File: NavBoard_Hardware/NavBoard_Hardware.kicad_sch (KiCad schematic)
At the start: 31 parts, among them J1 Conn_01x06_Male, U1 OKI-5V, U2 BHI160B, U3 ICM-20608-G, U4 OKI-3V3, U6 Raspberry_Pi

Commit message: Added title block info, adjusted powerpole connectors
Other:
- company: MRDT -> Missouri S&T Mars Rover Design Team
- title: NavBoard -> MRDT NavBoard
- moved on the sheet: Conn1A, Conn1B
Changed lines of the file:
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@@
   (paper "A4")
   (title_block
-    (title "NavBoard")
-    (rev "1")
-    (company "MRDT")
+    (title "MRDT NavBoard")
+    (date "2022-09-14")
+    (rev "2, 2023")
+    (company "Missouri S&T Mars Rover Design Team")
+    (comment 1 "Raspberry Pi Daughter Board")
+    (comment 2 "Contains Two Accelerometers & Connections To One UART GPS Module")
   )
   (junction (at 262.89 68.58) (diameter 0) (color 0 0 0 0)
@@
     (stroke (width 0) (type default) (color 0 0 0 0))
   )
+  (polyline (pts (xy 85.09 12.065) (xy 85.09 114.3))
+    (stroke (width 0) (type default) (color 0 0 0 0))
+  )
   (wire (pts (xy 246.38 148.59) (xy 246.38 151.13))
     (stroke (width 0) (type default) (color 0 0 0 0))
@@
     (stroke (width 0) (type default) (color 0 0 0 0))
   )
-  (wire (pts (xy 38.1 97.79) (xy 43.18 97.79))
+  (wire (pts (xy 36.83 97.79) (xy 31.75 97.79))
     (stroke (width 0) (type default) (color 0 0 0 0))
   )
@@
     (stroke (width 0) (type default) (color 0 0 0 0))
   )
-  (wire (pts (xy 66.04 97.79) (xy 71.12 97.79))
+  (wire (pts (xy 57.785 97.79) (xy 64.135 97.79))
     (stroke (width 0) (type default) (color 0 0 0 0))
   )
@@
     (stroke (width 0) (type default) (color 0 0 0 0))
   )
-  (wire (pts (xy 71.12 97.79) (xy 71.12 95.25))
+  (wire (pts (xy 64.135 97.79) (xy 64.135 95.25))
     (stroke (width 0) (type default) (color 0 0 0 0))
   )
@@
     (stroke (width 0) (type default) (color 0 0 0 0))
   )
-  (wire (pts (xy 43.18 97.79) (xy 43.18 100.33))
+  (wire (pts (xy 31.75 97.79) (xy 31.75 100.33))
     (stroke (width 0) (type default) (color 0 0 0 0))
   )
@@
     (effects (font (size 3.5052 3.5052) (thickness 0.701) bold italic) (justify left bottom))
   )
-  (text "Power" (at 43.18 20.32 0)
+  (text "Power" (at 38.735 20.32 0)
     (effects (font (size 3.5052 3.5052) (thickness 0.701) bold italic) (justify left bottom))
   )
@@
     (pin "1")
   )
-  (symbol (lib_id "MRDT_Connectors:AndersonPP") (at 27.94 100.33 0) (unit 1)
-    (in_bom yes) (on_board yes)
-    (property "Reference" "Conn1" (id 0) (at 33.2232 90.5002 0)
+  (symbol (lib_id "MRDT_Connectors:AndersonPP") (at 46.99 100.33 0) (mirror y) (unit 1)
+    (in_bom yes) (on_board yes)
+    (property "Reference" "Conn1" (id 0) (at 41.7068 90.5002 0)
       (effects (font (size 1.524 1.524)))
     )
-    (property "Value" "AndersonPP" (id 1) (at 33.2232 93.1926 0)
+    (property "Value" "AndersonPP" (id 1) (at 38.735 93.345 0)
       (effects (font (size 1.524 1.524)))
     )
-    (property "Footprint" "MRDT_Connectors:Anderson_2_Horizontal_Side_by_Side" (id 2) (at 24.13 114.3 0)
-      (effects (font (size 1.524 1.524)) hide)
-    )
-    (property "Datasheet" "" (id 3) (at 24.13 114.3 0)
-      (effects (font (size 1.524 1.524)) hide)
-    )
-    (pin "1")
-  )
-  (symbol (lib_id "MRDT_Connectors:AndersonPP") (at 55.88 100.33 0) (unit 2)
-    (in_bom yes) (on_board yes)
-    (property "Reference" "Conn1" (id 0) (at 61.1632 90.5002 0)
+    (property "Footprint" "MRDT_Connectors:Anderson_2_Horizontal_Side_by_Side" (id 2) (at 50.8 114.3 0)
+      (effects (font (size 1.524 1.524)) hide)
+    )
+    (property "Datasheet" "" (id 3) (at 50.8 114.3 0)
+      (effects (font (size 1.524 1.524)) hide)
+    )
+    (pin "1")
+  )
+  (symbol (lib_id "MRDT_Connectors:AndersonPP") (at 47.625 100.33 0) (unit 2)
+    (in_bom yes) (on_board yes)
+    (property "Reference" "Conn1" (id 0) (at 52.9082 90.5002 0)
       (effects (font (size 1.524 1.524)))
     )
-    (property "Value" "AndersonPP" (id 1) (at 61.1632 93.1926 0)
+    (property "Value" "AndersonPP" (id 1) (at 55.245 93.345 0)
       (effects (font (size 1.524 1.524)))
     )
-    (property "Footprint" "MRDT_Connectors:Anderson_2_Horizontal_Side_by_Side" (id 2) (at 52.07 114.3 0)
-      (effects (font (size 1.524 1.524)) hide)
-    )
-    (property "Datasheet" "" (id 3) (at 52.07 114.3 0)
+    (property "Footprint" "MRDT_Connectors:Anderson_2_Horizontal_Side_by_Side" (id 2) (at 43.815 114.3 0)
+      (effects (font (size 1.524 1.524)) hide)
+    )
+    (property "Datasheet" "" (id 3) (at 43.815 114.3 0)
       (effects (font (size 1.524 1.524)) hide)
     )
     (pin "2")
   )
-  (symbol (lib_id "power:GND") (at 43.18 100.33 0) (unit 1)
-    (in_bom yes) (on_board yes)
-    (property "Reference" "#PWR016" (id 0) (at 43.18 106.68 0)
-      (effects (font (size 1.27 1.27)) hide)
-    )
-    (property "Value" "GND" (id 1) (at 43.307 104.7242 0))
-    (property "Footprint" "" (id 2) (at 43.18 100.33 0)
-      (effects (font (size 1.27 1.27)) hide)
-    )
-    (property "Datasheet" "" (id 3) (at 43.18 100.33 0)
-      (effects (font (size 1.27 1.27)) hide)
-    )
-    (pin "1")
-  )
-  (symbol (lib_id "power:+12V") (at 71.12 95.25 0) (unit 1)
-    (in_bom yes) (on_board yes)
-    (property "Reference" "#PWR015" (id 0) (at 71.12 99.06 0)
-      (effects (font (size 1.27 1.27)) hide)
-    )
-    (property "Value" "+12V" (id 1) (at 71.501 90.8558 0))
-    (property "Footprint" "" (id 2) (at 71.12 95.25 0)
-      (effects (font (size 1.27 1.27)) hide)
-    )
-    (property "Datasheet" "" (id 3) (at 71.12 95.25 0)
-      (effects (font (size 1.27 1.27)) hide)
-    )
+  (symbol (lib_id "power:GND") (at 31.75 100.33 0) (mirror y) (unit 1)
+    (in_bom yes) (on_board yes)
+    (property "Reference" "#PWR016" (id 0) (at 31.75 106.68 0)
+      (effects (font (size 1.27 1.27)) hide)
+    )
+    (property "Value" "GND" (id 1) (at 31.623 104.7242 0))
+    (property "Footprint" "" (id 2) (at 31.75 100.33 0)
+      (effects (font (size 1.27 1.27)) hide)
+    )
+    (property "Datasheet" "" (id 3) (at 31.75 100.33 0)
+      (effects (font (size 1.27 1.27)) hide)
+    )
+    (pin "1")
+  )
+  (symbol (lib_id "power:+12V") (at 64.135 95.25 0) (unit 1)
+    (in_bom yes) (on_board yes)
+    (property "Reference" "#PWR015" (id 0) (at 64.135 99.06 0)
+      (effects (font (size 1.27 1.27)) hide)
+    )
+    (property "Value" "+12V" (id 1) (at 64.516 90.8558 0))
+    (property "Footprint" "" (id 2) (at 64.135 95.25 0)
+      (effects (font (size 1.27 1.27)) hide)
+    )
+    (property "Datasheet" "" (id 3) (at 64.135 95.25 0)
+      (effects (font (size 1.27 1.27)) hide)
+    )

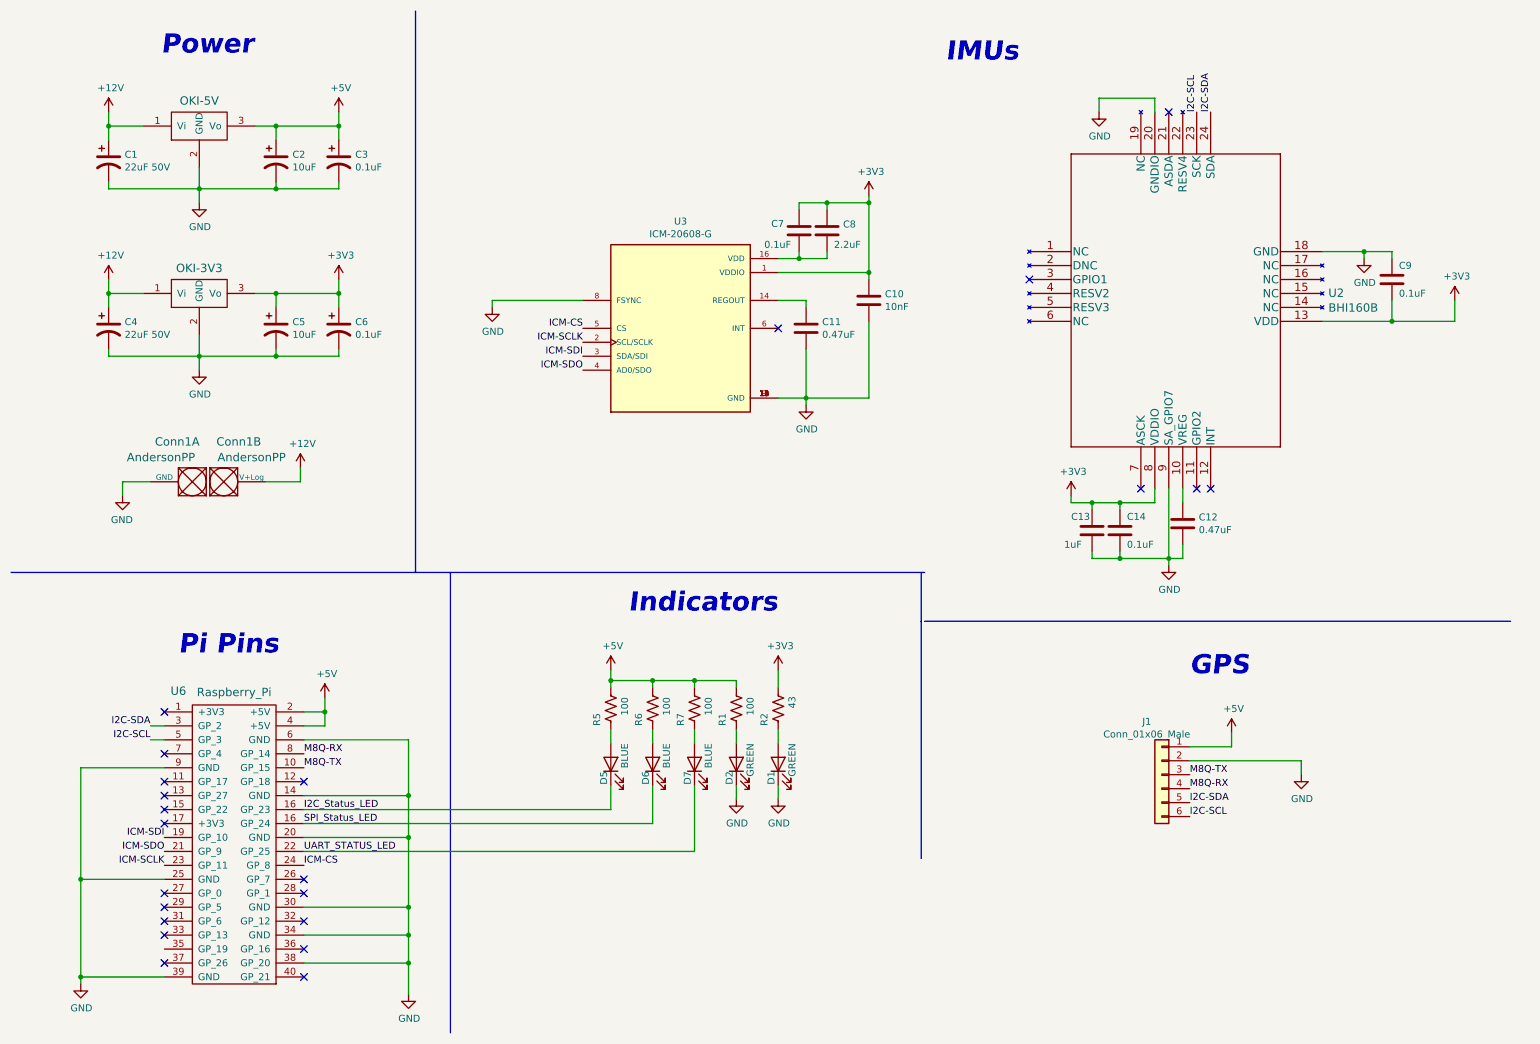
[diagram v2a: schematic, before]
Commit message: Added test points and pulldown resistors to unused pins of ICM-20608
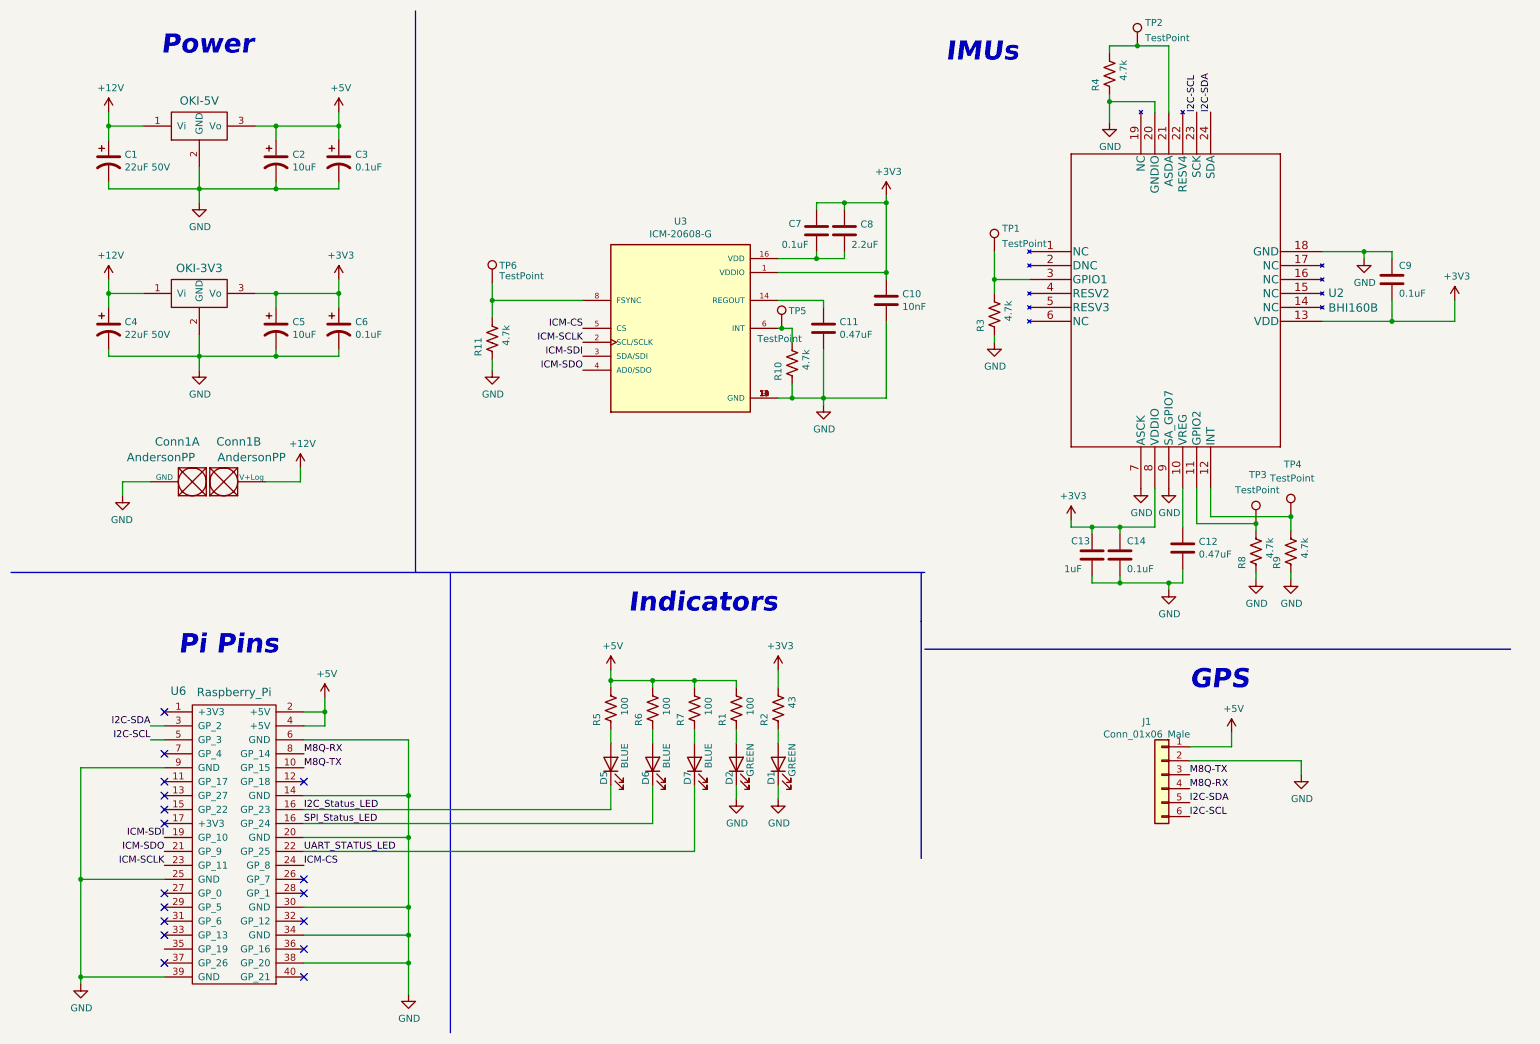
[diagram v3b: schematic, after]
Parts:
- added R10, R11, R3, R4, R8, R9: 4.7k, Resistor_SMD:R_0603_1608Metric_Pad0.98x0.95mm_HandSolder, symbol Device:R_US
- added TP1, TP2, TP3, TP4, TP5, TP6: TestPoint, TestPoint:TestPoint_Pad_D2.0mm, symbol Connector:TestPoint
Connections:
- net GND: now also U2.7 (ASCK), R10.2, R11.2, R3.2, R4.2, R8.2, R9.2; no longer U3.8 (FSYNC)
- net at U3.6 (INT): now also R10.1, TP5.1
- net at U2.11 (GPIO2): now also R8.1, TP3.1
- net at U2.12 (INT): now also R9.1, TP4.1
- net at U2.21 (ASDA): now also R4.1, TP2.1
- net at U2.3 (GPIO1): now also R3.1, TP1.1
- new net: R11.1, TP6.1, U3.8 (FSYNC)
- no-connect marks 23 -> 17
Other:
- moved on the sheet: C10, C11, C12, C13, C14, C7, C8

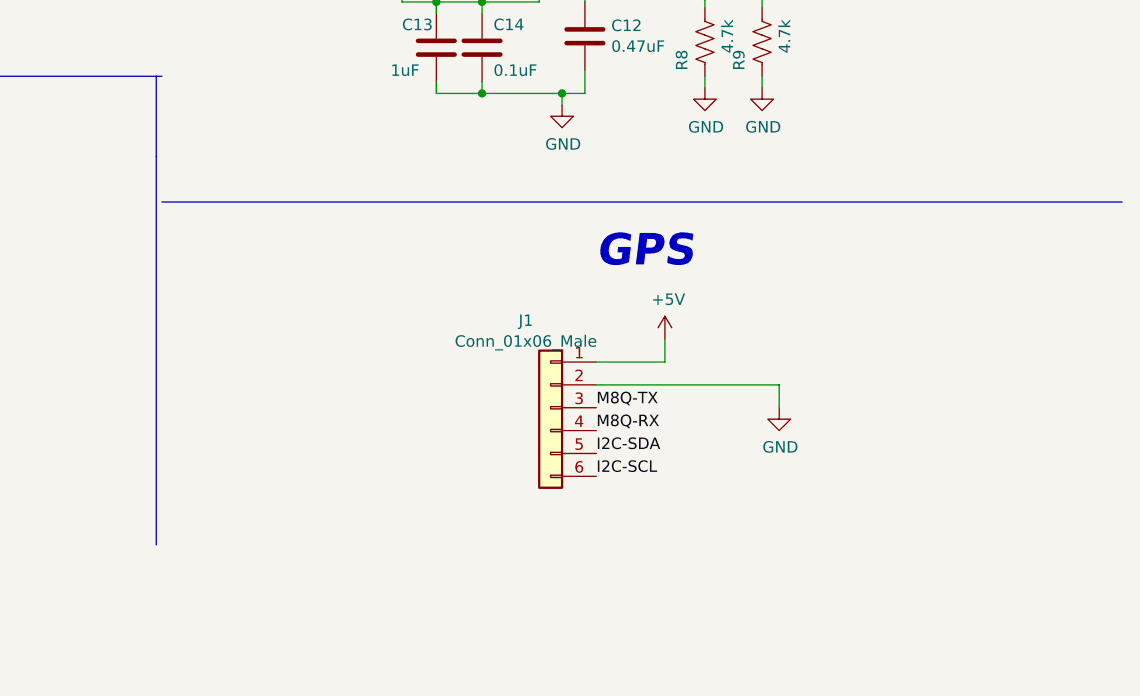
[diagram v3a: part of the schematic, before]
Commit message: Routed most components
Some power traces, and LEDs remain
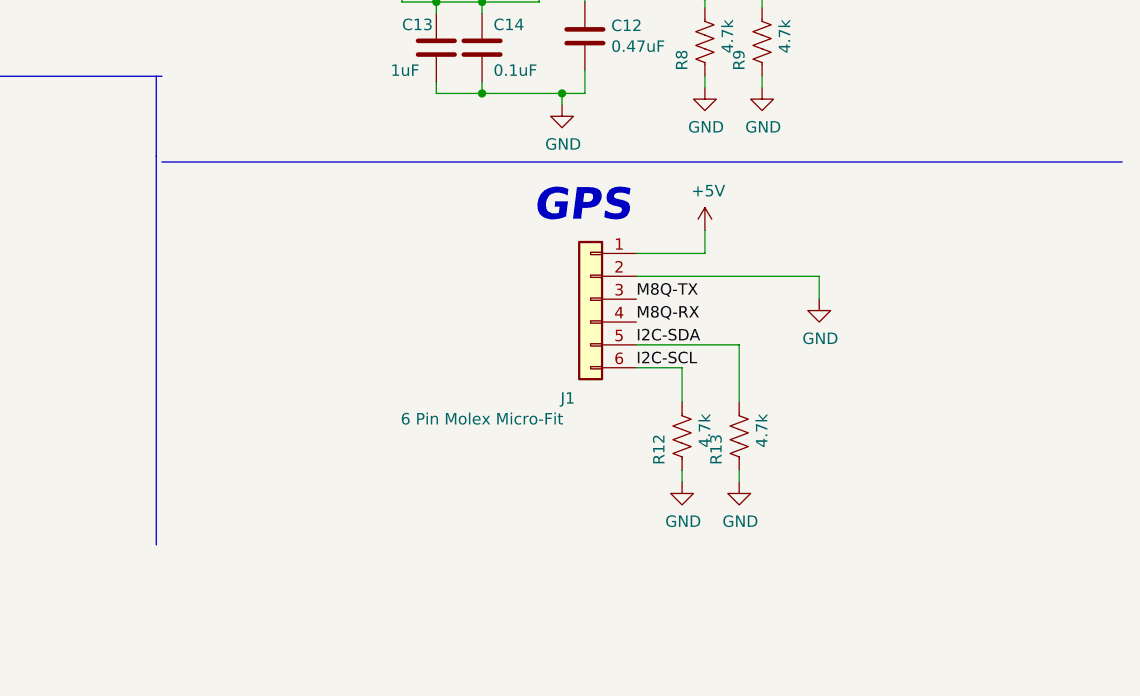
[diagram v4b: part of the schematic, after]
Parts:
- added R12, R13: 4.7k, Resistor_SMD:R_0603_1608Metric_Pad0.98x0.95mm_HandSolder, symbol Device:R_US
- J1: value Conn_01x06_Male -> 6 Pin Molex Micro-Fit
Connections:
- net GND: now also R12.2, R13.2
- net I2C-SCL: now also R12.1
- net I2C-SDA: now also R13.1
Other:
- moved on the sheet: J1
